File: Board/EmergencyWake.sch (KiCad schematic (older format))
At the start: 140 parts, among them J1 USB_C_Receptacle_USB2.0, J10 Conn_01x04, J2 Micro_SD_Card_Det, J3 Conn_01x03, J4 Conn_01x02, J5 Conn_01x05, J6 Conn_01x04, J7 Conn_01x02, J8 Conn_01x04, J9 Conn_01x04, Q1 AO3400A, Q2 AO3401A, Q3 AO3400A, SW1 SW_DPDT_x2, SW2 SW_Push, SW3 SW_Push, SW4 SW_Push, U1 M24C02-WMN, U10 L9110S, U11 SRV05-4, U2 AMS1117-3.3, U3 MC34063AD, U4 STM32F407VETx, U5 LM4670, U6 173950378, U7 PT6312B, U8 EL357N-G, U9 EL357N-G, Y1 32,768

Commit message: [Board] Added OR gate for wakeup signal
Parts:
- added Q4, Q5: AO3401A, Package_TO_SOT_SMD:SOT-23, symbol Device:Q_PMOS_GSD
- added R49, R50: 100k, Resistor_SMD:R_0402_1005Metric, symbol Device:R
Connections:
- net GND: now also J4.2 (Pin_2), R50.1; no longer R30.2
- net I2C_INT: now also Q5.1 (G), R49.1
- net LEVER: now also Q4.1 (G); no longer U4.23 (PA0)
- net VCC: now also R30.2, Q4.2 (S), Q5.2 (S), R49.2; no longer J4.2 (Pin_2)
- new net WAKEUP: Q4.3 (D), Q5.3 (D), R50.2, U4.23 (PA0)
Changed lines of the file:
@@
 $EndComp
 $Comp
-L power:GND #PWR060
-U 1 1 5E40A4BA
-P 11900 2450
-F 0 "#PWR060" H 11900 2200 50  0001 C CNN
-F 1 "GND" H 11905 2277 50  0000 C CNN
-F 2 "" H 11900 2450 50  0001 C CNN
-F 3 "" H 11900 2450 50  0001 C CNN
-	1    11900 2450
-	0    1    1    0
-$EndComp
-$Comp
 L power:GND #PWR063
 U 1 1 5E40A893
@@
 $EndComp
 $Comp
-L Device:R R30
-U 1 1 5E637187
-P 12050 2450
-F 0 "R30" V 12150 2450 50  0000 C CNN
-F 1 "100k" V 11950 2450 50  0000 C CNN
-F 2 "Resistor_SMD:R_0402_1005Metric" V 11980 2450 50  0001 C CNN
-F 3 "~" H 12050 2450 50  0001 C CNN
-F 4 "C25741" H 12050 2450 50  0001 C CNN "LCSC"
-	1    12050 2450
-	0    1    -1   0
-$EndComp
-$Comp
 L Device:C C29
 U 1 1 5E637192
@@
 $EndComp
 Wire Wire Line
-	12200 2850 12250 2850
-Wire Wire Line
-	12250 2850 12250 2450
-Wire Wire Line
-	12250 2850 13700 2850
-Wire Wire Line
 	12250 2000 12200 2000
 Wire Wire Line
@@
 Wire Wire Line
 	8950 8100 9350 8100
-Wire Wire Line
-	8950 3300 9050 3300
-Wire Wire Line
-	9050 3300 9050 3200
-Connection ~ 9050 3200
 NoConn ~ 8950 3400
 NoConn ~ 8950 4000
@@
 $EndComp
 $Comp
-L power:VCC #PWR048
-U 1 1 5E63717C
-P 13700 2950
-F 0 "#PWR048" H 13700 2800 50  0001 C CNN
-F 1 "VCC" V 13718 3077 50  0000 L CNN
-F 2 "" H 13700 2950 50  0001 C CNN
-F 3 "" H 13700 2950 50  0001 C CNN
-	1    13700 2950
-	0    -1   -1   0
-$EndComp
-$Comp
 L power:GND #PWR059
 U 1 1 5E40A111
@@
 Wire Wire Line
 	2550 4500 4950 4500
-Wire Wire Line
-	12200 2450 12250 2450
 $Comp
 L MCU_ST_STM32F4:STM32F407VETx U4
@@
 Wire Wire Line
 	7150 3200 6600 3200
-Wire Wire Line
-	8950 3200 9050 3200
 Text Label 9850 3600 2    50   ~ 0
 AUDIO_OUT
@@
 Wire Wire Line
 	8950 3500 9850 3500
-Text Label 9850 3200 2    50   ~ 0
+Text Label 9850 3300 2    50   ~ 0
 LEVER
-Wire Wire Line
-	9050 3200 9850 3200
 $Comp
 L Device:C C35
@@
 Text Label 12550 1750 0    50   ~ 0
 I2C_INT
-Connection ~ 12250 2850
 Wire Wire Line
 	12250 1600 12250 2000
@@
 	0    -1   -1   0
 $EndComp
+$Comp
+L Device:Q_PMOS_GSD Q4
+U 1 1 5E5C735D
+P 14600 2500
+F 0 "Q4" V 14900 2500 50  0000 C CNN
+F 1 "AO3401A" V 14800 2500 50  0000 C CNN
+F 2 "Package_TO_SOT_SMD:SOT-23" H 14800 2600 50  0001 C CNN
+F 3 "https://datasheet.lcsc.com/szlcsc/Alpha-Omega-Semicon-AOS-AO3401A_C15127.pdf" H 14600 2500 50  0001 C CNN
+F 4 "C15127" V 14600 2500 50  0001 C CNN "LCSC"
+	1    14600 2500
+	1    0    0    1
+$EndComp
+$Comp
+L Device:Q_PMOS_GSD Q5
+U 1 1 5E5CCD6C
+P 15600 2500
+F 0 "Q5" V 15900 2500 50  0000 C CNN
+F 1 "AO3401A" V 15800 2500 50  0000 C CNN
+F 2 "Package_TO_SOT_SMD:SOT-23" H 15800 2600 50  0001 C CNN
+F 3 "https://datasheet.lcsc.com/szlcsc/Alpha-Omega-Semicon-AOS-AO3401A_C15127.pdf" H 15600 2500 50  0001 C CNN
+F 4 "C15127" V 15600 2500 50  0001 C CNN "LCSC"
+	1    15600 2500
+	1    0    0    1
+$EndComp
+Wire Wire Line
+	14700 2700 14700 2750
+Wire Wire Line
+	15700 2700 15700 2750
+Connection ~ 15700 2750
+Wire Wire Line
+	15400 2500 15350 2500
+Wire Wire Line
+	14400 2500 14350 2500
+$Comp
+L Device:R R30
+U 1 1 5E7C70C9
+P 14350 2300
+F 0 "R30" V 14450 2250 50  0000 L CNN
+F 1 "100k" V 14250 2200 50  0000 L CNN
+F 2 "Resistor_SMD:R_0402_1005Metric" V 14280 2300 50  0001 C CNN
+F 3 "~" H 14350 2300 50  0001 C CNN
+F 4 "C25741" H 14350 2300 50  0001 C CNN "LCSC"
+	1    14350 2300
+	-1   0    0    1
+$EndComp
+$Comp
+L Device:R R49
+U 1 1 5E7C73C0
+P 15350 2300
+F 0 "R49" V 15450 2250 50  0000 L CNN
+F 1 "100k" V 15250 2200 50  0000 L CNN
+F 2 "Resistor_SMD:R_0402_1005Metric" V 15280 2300 50  0001 C CNN
+F 3 "~" H 15350 2300 50  0001 C CNN
+F 4 "C25741" H 15350 2300 50  0001 C CNN "LCSC"
+	1    15350 2300
+	-1   0    0    1
+$EndComp
+Wire Wire Line
+	15350 2450 15350 2500
+Connection ~ 15350 2500
+Wire Wire Line
+	15350 2500 15000 2500
+Wire Wire Line
+	14350 2450 14350 2500
+Connection ~ 14350 2500
+Wire Wire Line
+	14350 2500 14050 2500
+Wire Wire Line
+	14350 2150 14350 2100
+Wire Wire Line
+	14350 2100 14700 2100
+Wire Wire Line
+	14700 2100 14700 2300
+Wire Wire Line
+	15350 2150 15350 2100
+Wire Wire Line
+	15350 2100 15700 2100
+Wire Wire Line
+	15700 2100 15700 2300
+Wire Wire Line
+	14700 2100 15350 2100
+Connection ~ 14700 2100
+Connection ~ 15350 2100
+Wire Wire Line
+	14700 2100 14700 2050
+$Comp
+L power:VCC #PWR060
+U 1 1 5EA924E1
+P 14700 2050
+F 0 "#PWR060" H 14700 1900 50  0001 C CNN
+F 1 "VCC" V 14718 2177 50  0000 L CNN
+F 2 "" H 14700 2050 50  0001 C CNN
+F 3 "" H 14700 2050 50  0001 C CNN
+	1    14700 2050
+	1    0    0    -1
+$EndComp
+$Comp
+L power:GND #PWR072
+U 1 1 5EA9392E
+P 15700 3150
+F 0 "#PWR072" H 15700 2900 50  0001 C CNN
+F 1 "GND" H 15705 2977 50  0000 C CNN
+F 2 "" H 15700 3150 50  0001 C CNN
+F 3 "" H 15700 3150 50  0001 C CNN
+	1    15700 3150
+	1    0    0    -1
+$EndComp
+Wire Wire Line
+	12200 2850 13700 2850
+$Comp
+L power:GND #PWR048
+U 1 1 5EA9AD8A
+P 13700 2950
+F 0 "#PWR048" H 13700 2700 50  0001 C CNN
+F 1 "GND" H 13705 2777 50  0000 C CNN
+F 2 "" H 13700 2950 50  0001 C CNN
+F 3 "" H 13700 2950 50  0001 C CNN
+	1    13700 2950
+	0    1    1    0
+$EndComp
+Text Label 14050 2500 0    50   ~ 0
+LEVER
+Text Label 15000 2500 0    50   ~ 0
+I2C_INT
+Text Label 15450 2750 2    50   ~ 0
+WAKEUP
+Wire Wire Line
+	14700 2750 15700 2750
+$Comp
+L Device:R R50
+U 1 1 5E5D17DB
+P 15700 2950
+F 0 "R50" V 15800 2900 50  0000 L CNN
+F 1 "100k" V 15600 2850 50  0000 L CNN
+F 2 "Resistor_SMD:R_0402_1005Metric" V 15630 2950 50  0001 C CNN
+F 3 "~" H 15700 2950 50  0001 C CNN
+F 4 "C25741" H 15700 2950 50  0001 C CNN "LCSC"
+	1    15700 2950
+	-1   0    0    1
+$EndComp
+Wire Wire Line
+	15700 3150 15700 3100
+Wire Wire Line
+	15700 2800 15700 2750
+Text Label 9850 3200 2    50   ~ 0
+WAKEUP
+Wire Wire Line
+	8950 3200 9850 3200
+Wire Wire Line
+	8950 3300 9850 3300
 $EndSCHEMATC

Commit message: [Board] New fabrication files
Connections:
- net VCC: no longer TP4.1
- net at C13.1, D5.1 (K), JP6.1 (A)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: now also TP4.1
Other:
- moved on the sheet: TP4
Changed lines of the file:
@@
 L Connector:TestPoint TP4
 U 1 1 5EB86E6F
-P 5000 900
-F 0 "TP4" H 5058 1018 50  0000 L CNN
-F 1 "VCC" H 5058 927 50  0000 L CNN
-F 2 "TestPoint:TestPoint_Loop_D1.80mm_Drill1.0mm_Beaded" H 5200 900 50  0001 C CNN
-F 3 "~" H 5200 900 50  0001 C CNN
-	1    5000 900
+P 5550 1350
+F 0 "TP4" H 5608 1468 50  0000 L CNN
+F 1 "VCC" H 5608 1377 50  0000 L CNN
+F 2 "TestPoint:TestPoint_Loop_D1.80mm_Drill1.0mm_Beaded" H 5750 1350 50  0001 C CNN
+F 3 "~" H 5750 1350 50  0001 C CNN
+	1    5550 1350
 	-1   0    0    -1
 $EndComp
@@
 	5250 1200 5250 1350
 Wire Wire Line
-	5250 1350 5650 1350
-Wire Wire Line
-	5000 900  5250 900
-Connection ~ 5250 900
+	5250 1350 5550 1350
 $Comp
 L Connector:TestPoint TP1
@@
 Wire Wire Line
 	8950 3300 9850 3300
+Connection ~ 5550 1350
+Wire Wire Line
+	5550 1350 5650 1350
 $EndSCHEMATC

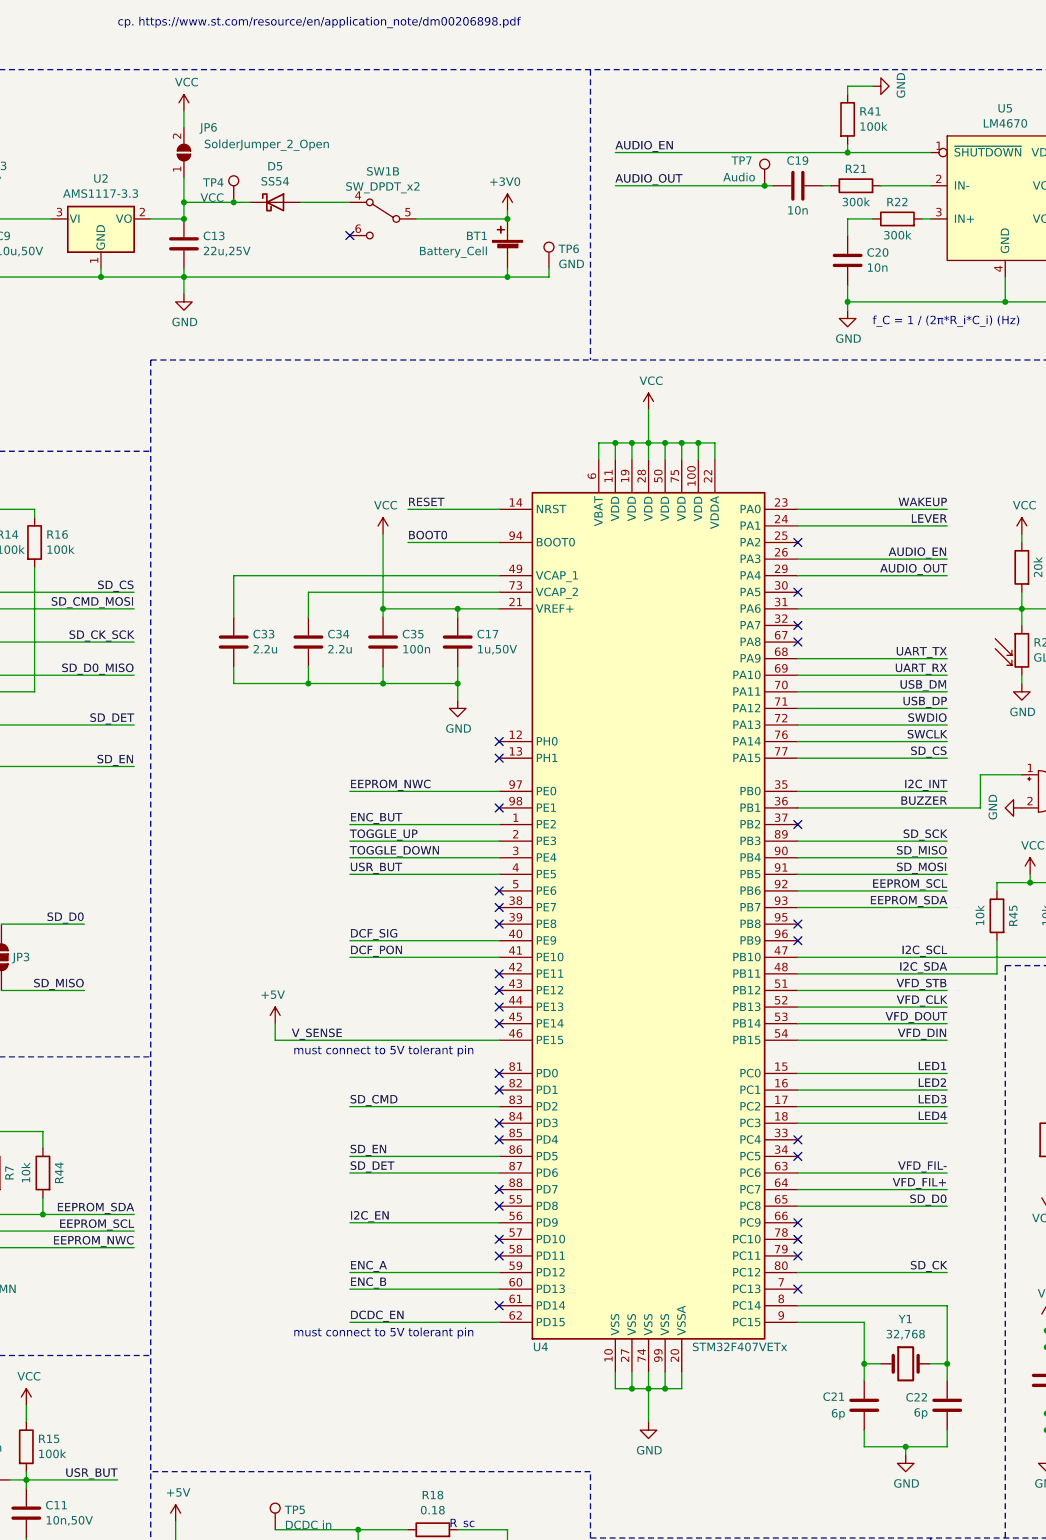
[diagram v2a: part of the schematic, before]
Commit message: [Board] Corrected assembly information for JLCPCB
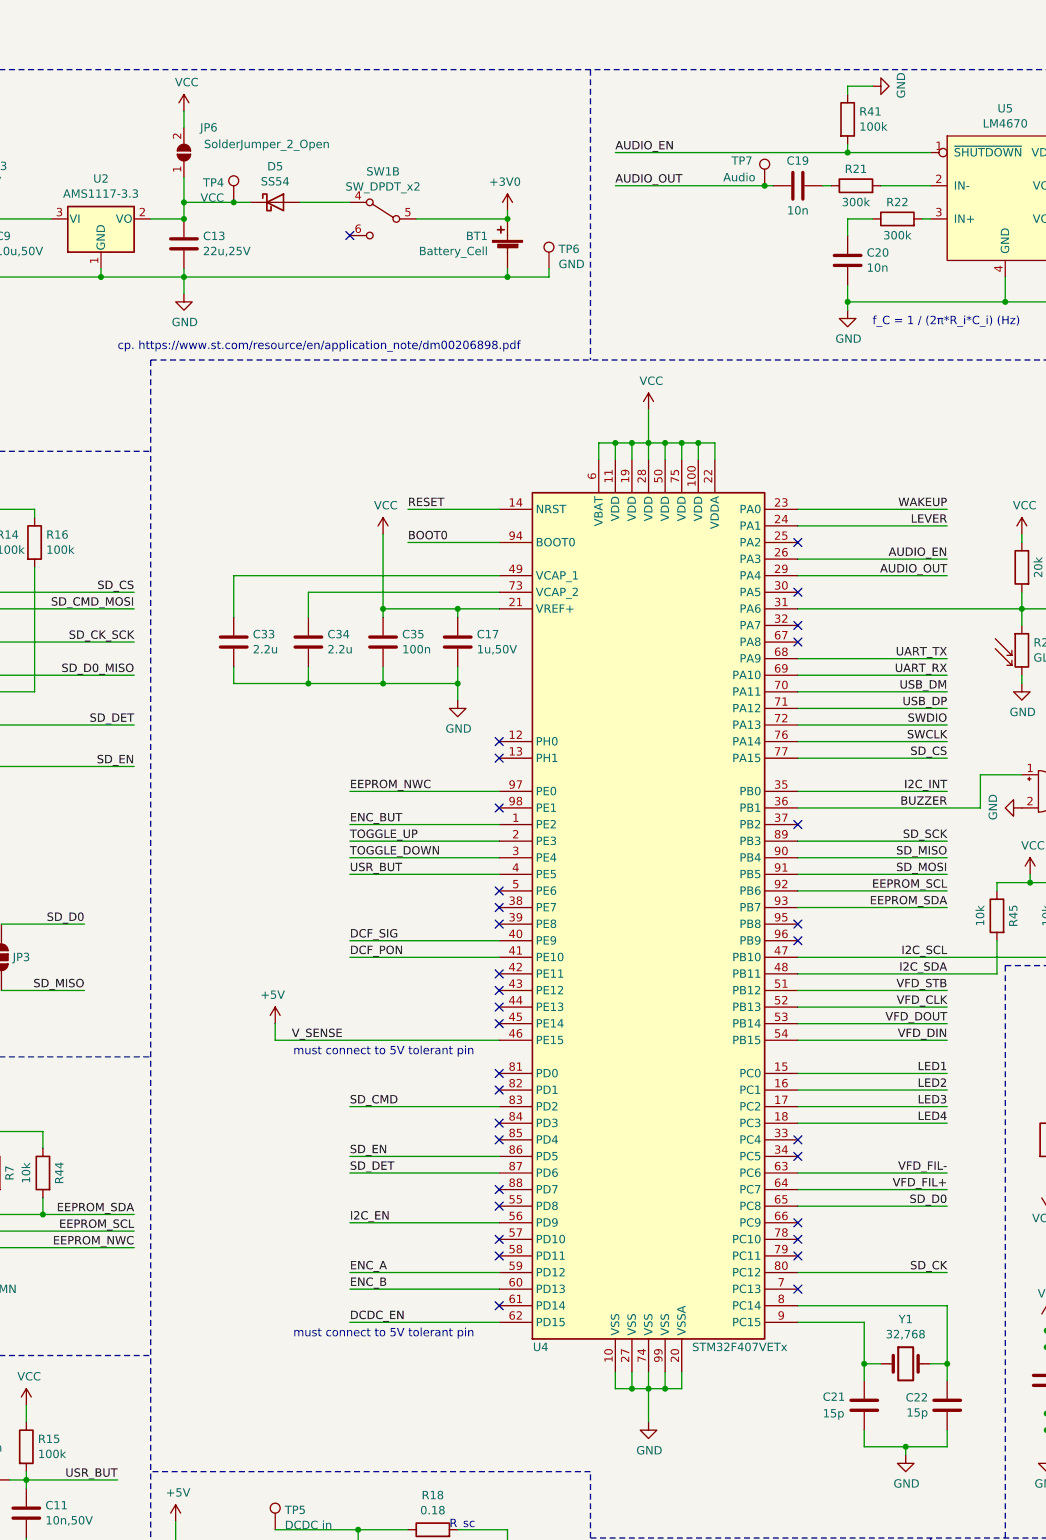
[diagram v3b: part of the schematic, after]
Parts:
- C21, C22: value 6p -> 15p; LCSC C37474 -> C1548
- Y1: LCSC C94673 -> C32346
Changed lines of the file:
@@
 F 2 "Crystal:Crystal_SMD_3215-2Pin_3.2x1.5mm" H 9600 8350 50  0001 C CNN
 F 3 "~" H 9600 8350 50  0001 C CNN
-F 4 "C94673" H 9600 8350 50  0001 C CNN "LCSC"
+F 4 "C32346" H 9600 8350 50  0001 C CNN "LCSC"
 	1    9600 8350
 	1    0    0    -1
@@
 P 9350 8600
 F 0 "C21" H 9100 8650 50  0000 L CNN
-F 1 "6p" H 9150 8550 50  0000 L CNN
+F 1 "15p" H 9100 8550 50  0000 L CNN
 F 2 "Capacitor_SMD:C_0402_1005Metric" H 9388 8450 50  0001 C CNN
 F 3 "~" H 9350 8600 50  0001 C CNN
-F 4 "C37474" H 9350 8600 50  0001 C CNN "LCSC"
+F 4 "C1548" H 9350 8600 50  0001 C CNN "LCSC"
 	1    9350 8600
 	1    0    0    -1
@@
 P 9850 8600
 F 0 "C22" H 9965 8646 50  0000 L CNN
-F 1 "6p" H 9965 8555 50  0000 L CNN
+F 1 "15p" H 9965 8555 50  0000 L CNN
 F 2 "Capacitor_SMD:C_0402_1005Metric" H 9888 8450 50  0001 C CNN
 F 3 "~" H 9850 8600 50  0001 C CNN
-F 4 "C37474" H 9850 8600 50  0001 C CNN "LCSC"
+F 4 "C1548" H 9850 8600 50  0001 C CNN "LCSC"
 	1    9850 8600
 	-1   0    0    -1
@@
 Wire Wire Line
 	4000 1450 4450 1450
-Text Notes 4850 300  0    50   ~ 0
+Text Notes 4850 2250 0    50   ~ 0
 cp. https://www.st.com/resource/en/application_note/dm00206898.pdf
 $Comp

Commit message: [Board] Some minor changes
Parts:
- added C36: 22u,25V, Capacitor_SMD:C_0805_2012Metric, symbol Device:C
- C26: value 10u,50V -> 10u,25V
- C9: value 10u,50V -> 10u,25V; footprint Capacitor_SMD:C_1206_3216Metric -> Capacitor_SMD:C_0805_2012Metric; LCSC C13585 -> C15850
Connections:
- net +5V: now also C24.1, U5.7 (VDD)
- net GND: now also C36.1
- net VCC: now also C36.2; no longer C24.1, U5.7 (VDD)
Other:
- moved on the sheet: J2, JP1, JP2, JP3, Q1, R10, R11, R12, R13, R14, R16, R9

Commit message: [Board] Replaced audio amplifier
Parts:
- removed R21, R22: 300k, Resistor_SMD:R_0603_1608Metric, symbol Device:R
- removed R41: 100k, Resistor_SMD:R_0402_1005Metric, symbol Device:R
- removed TP7: Audio, TestPoint:TestPoint_Loop_D1.80mm_Drill1.0mm_Beaded, symbol Connector:TestPoint
- removed U5: LM4670, Package_SON:WSON-8-1EP_3x3mm_P0.5mm_EP1.6x2.0mm, symbol Amplifier:LM4670
- added C37, C38, C39: 100n, Capacitor_SMD:C_0402_1005Metric, symbol Device:C
- added JP7: SolderJumper_3_Open, Jumper:SolderJumper-3_P1.3mm_Open_RoundedPad1.0x1.5mm_NumberLabels, symbol Jumper:SolderJumper_3_Open
- added U5: WM8960, Package_DFN_QFN:QFN-32-1EP_5x5mm_P0.5mm_EP3.45x3.45mm, symbol Amplifier:WM8960
- added Y2: 8M, Crystal:Crystal_SMD_5032-2Pin_5.0x3.2mm, symbol Device:Crystal
- C19, C20: value 10n -> 30p; footprint Capacitor_SMD:C_0603_1608Metric -> Capacitor_SMD:C_0402_1005Metric; LCSC C57112 -> C1570
- C24: value 1u,50V -> 10u,25V; footprint Capacitor_SMD:C_0603_1608Metric -> Capacitor_SMD:C_0805_2012Metric; LCSC C15849 -> C15850
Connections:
- net +5V: now also JP7.3 (B); no longer C24.1
- net GND: now also C19.2, C20.2, C37.2, C38.2, C39.2, U5.20 (SPKGND2), U5.24 (SPKGND1), U5.28 (AGND), U5.33 (GND_PAD), U5.9 (DGND); no longer C20.1
- net I2C_SCL: now also U5.17 (SCLK)
- net I2C_SDA: now also U5.18 (SDIN)
- net SD_CS: now also U4.29 (PA4); no longer U4.77 (PA15)
- net SD_MOSI: now also U4.32 (PA7); no longer U4.91 (PB5)
- net SD_SCK: now also U4.30 (PA5); no longer U4.89 (PB3)
- net VCC: now also C37.1, C38.1, C39.1, JP7.1 (A), U5.10 (DBVDD), U5.32 (AVDD), U5.8 (DCVDD)
- net at U4.12 (PH0): now also C19.1, Y2.1
- net at U4.13 (PH1): now also C20.1, Y2.2
- net MCLK: now reaches U4.66 (PC9)
- net MCLK: now also U5.11 (MCLK)
- net I2S_CK: now reaches U4.78 (PC10)
- net I2S_CK: now also U5.12 (BCLK)
- net I2S_extSD: now reaches U4.79 (PC11)
- net AUDIO_EN: no longer names the net of U4.26 (PA3)
- removed net AUDIO_OUT: C19.2, U4.29 (PA4)
- net SP+ renamed SPK_LP
- net SPK_LP: now also U5.25 (SPK_LP)
- net SP- renamed SPK_LN
- net SPK_LN: now also U5.23 (SPK_LN)
- new net: C24.1, JP7.2 (C), U5.21 (SPKVDD2), U5.26 (SPKVDD1)
- new net I2S_SD: U4.91 (PB5), U5.14 (DACDAT)
- new net I2S_WS: U4.77 (PA15), U5.13 (DACLRC)
- no-connect marks 56 -> 67
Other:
- note added: "Additional circuitry for STM32"
- note added: "Audio amplifier\nI2C address: 0x34"
- note added: "Audio output can be directly wired to the\nspeaker if wires are shorter than 100 mm."
- note added: "Both LEVER and I2C_INT can generate a \nrising edge on WAKEUP pin of STM32\n(both signals are active low)."
- note added: "EEPROM uses a\nseperate I2C bus"
- note added: "Filament voltage"
- note added: "For more information on backup battery circuit:\nhttps://www.st.com/resource/en/application_note/dm00206898.pdf"
- note added: "HSE is necessary for USB"
- note added: "I2C bus is used for proximity\nsensor and audio amplifier."
- note added: "Jumpers select between SDIO and SPI signals for SD card\n1) SDIO - 2) SPI"
- note added: "LSE is necessary for accurate RTC"
- note added: "Option to permanently enable DCDC (for testing without STM32)"
- note added: "Proximity sensor (APDS 9960)\nI2C address: 0x39"
- note added: "SD card can be powered down with this low side switch"
- note added: "Speaker\n8 ohms"
- note removed: "Proximity sensor"
- note removed: "Speaker"
- note removed: "cp. https://www.st.com/resource/en/application_note/dm00206898.pdf"
- note removed: "f_C = 1 / (2π*R_i*C_i) (Hz)"
- moved on the sheet: BT1, BZ1, C1, C10, C11, C12, C13, C14, C15, C16, C17, C18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

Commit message: [Board] Minor Layout changes
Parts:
- added TP7: MCLK, TestPoint:TestPoint_Loop_D1.80mm_Drill1.0mm_Beaded, symbol Connector:TestPoint
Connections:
- net MCLK: now also TP7.1
- net I2C_EN renamed PROX_EN
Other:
- note added: "Grid 3 can either be permanently\nactive or be driven together with\nGrid 2 (selectable by solder jumper)"
- note removed: "Grid 3 can either be permanently\nactive be driven together with\nGrid 2 (selectable by solder jumper)"
- moved on the sheet: R42
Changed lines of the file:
@@
 EESchema Schematic File Version 4
+LIBS:EmergencyWake-cache
 EELAYER 30 0
 EELAYER END
@@
 	-1   0    0    1
 $EndComp
-Text Notes 22050 11950 1    50   ~ 0
-Grid 3 can either be permanently\nactive be driven together with\nGrid 2 (selectable by solder jumper)
+Text Notes 21400 11000 0    50   ~ 0
+Grid 3 can either be permanently\nactive or be driven together with\nGrid 2 (selectable by solder jumper)
 Connection ~ 21400 11950
 $Comp
@@
 	0    1    1    0
 $EndComp
-$Comp
-L power:VCC #PWR038
-U 1 1 5FFA697A
-P 16900 10800
-F 0 "#PWR038" H 16900 10650 50  0001 C CNN
-F 1 "VCC" H 16917 10973 50  0000 C CNN
-F 2 "" H 16900 10800 50  0001 C CNN
-F 3 "" H 16900 10800 50  0001 C CNN
-	1    16900 10800
-	0    -1   -1   0
-$EndComp
-Wire Wire Line
-	16900 10800 17000 10800
 Text Label 16900 11000 0    50   ~ 0
 VFD_DIN
@@
 Wire Wire Line
 	18750 6950 20050 6950
-$Comp
-L Device:R R42
-U 1 1 5E477866
-P 16700 11450
-F 0 "R42" H 16770 11496 50  0000 L CNN
-F 1 "100k" H 16770 11405 50  0000 L CNN
-F 2 "Resistor_SMD:R_0402_1005Metric" V 16630 11450 50  0001 C CNN
-F 3 "~" H 16700 11450 50  0001 C CNN
-F 4 "C25741" H 16700 11450 50  0001 C CNN "LCSC"
-	1    16700 11450
-	1    0    0    -1
-$EndComp
-$Comp
-L power:VCC #PWR0101
-U 1 1 5E678EA5
-P 16700 11750
-F 0 "#PWR0101" H 16700 11600 50  0001 C CNN
-F 1 "VCC" H 16717 11923 50  0000 C CNN
-F 2 "" H 16700 11750 50  0001 C CNN
-F 3 "" H 16700 11750 50  0001 C CNN
-	1    16700 11750
-	-1   0    0    1
-$EndComp
-Wire Wire Line
-	16700 11600 16700 11750
 Wire Wire Line
 	17400 11300 16900 11300
@@
 NoConn ~ 17800 13600
 NoConn ~ 17400 11550
-Wire Wire Line
-	16700 11100 16700 11300
 $Comp
 L VFD:PT6312B U7
@@
 	19600 5650 19250 5650
 Text Label 18900 5650 0    50   ~ 0
-I2C_EN
+PROX_EN
 Wire Wire Line
 	19900 5450 19900 5400
@@
 I2C_SDA
 Text Label 8350 9200 0    50   ~ 0
-I2C_EN
+PROX_EN
 Wire Wire Line
 	9250 9200 8350 9200
@@
 	10550 14350 10550 15100
 Wire Wire Line
-	10550 15100 9450 15100
-Wire Wire Line
 	10850 14350 10850 15200
 Wire Wire Line
@@
 	1    0    0    -1
 $EndComp
+$Comp
+L Device:R R42
+U 1 1 5E477866
+P 16700 10950
+F 0 "R42" H 16770 10996 50  0000 L CNN
+F 1 "100k" H 16770 10905 50  0000 L CNN
+F 2 "Resistor_SMD:R_0402_1005Metric" V 16630 10950 50  0001 C CNN
+F 3 "~" H 16700 10950 50  0001 C CNN
+F 4 "C25741" H 16700 10950 50  0001 C CNN "LCSC"
+	1    16700 10950
+	-1   0    0    1
+$EndComp
+Wire Wire Line
+	16400 10800 16700 10800
+$Comp
+L power:VCC #PWR038
+U 1 1 5FFA697A
+P 16400 10800
+F 0 "#PWR038" H 16400 10650 50  0001 C CNN
+F 1 "VCC" H 16417 10973 50  0000 C CNN
+F 2 "" H 16400 10800 50  0001 C CNN
+F 3 "" H 16400 10800 50  0001 C CNN
+	1    16400 10800
+	0    -1   -1   0
+$EndComp
+Connection ~ 16700 10800
+Wire Wire Line
+	16700 10800 17000 10800
+$Comp
+L Connector:TestPoint TP7
+U 1 1 5E81CC9A
+P 9150 15100
+F 0 "TP7" H 9208 15218 50  0000 L CNN
+F 1 "MCLK" H 9208 15127 50  0000 L CNN
+F 2 "TestPoint:TestPoint_Loop_D1.80mm_Drill1.0mm_Beaded" H 9350 15100 50  0001 C CNN
+F 3 "~" H 9350 15100 50  0001 C CNN
+	1    9150 15100
+	1    0    0    -1
+$EndComp
+Wire Wire Line
+	9150 15100 10550 15100
 $EndSCHEMATC
